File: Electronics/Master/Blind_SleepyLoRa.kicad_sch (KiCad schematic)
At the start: 12 parts, among them J1 Conn_01x04_Socket, J2 Conn_01x04_Socket, J3 Conn_01x04_Socket, SW1 SW_Omron_B3FS

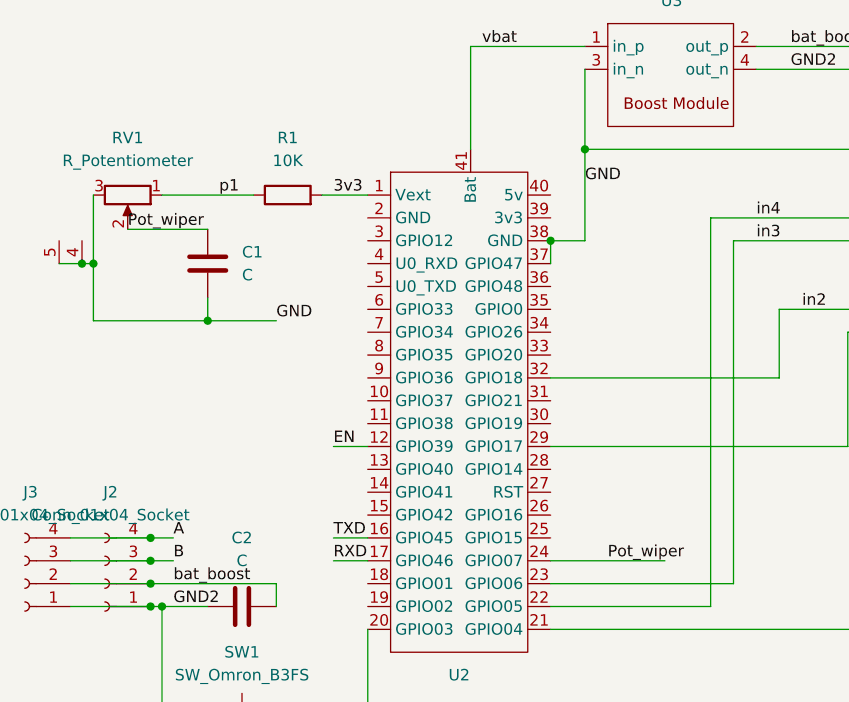
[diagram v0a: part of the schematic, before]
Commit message: Update master PCB to include ref voltage
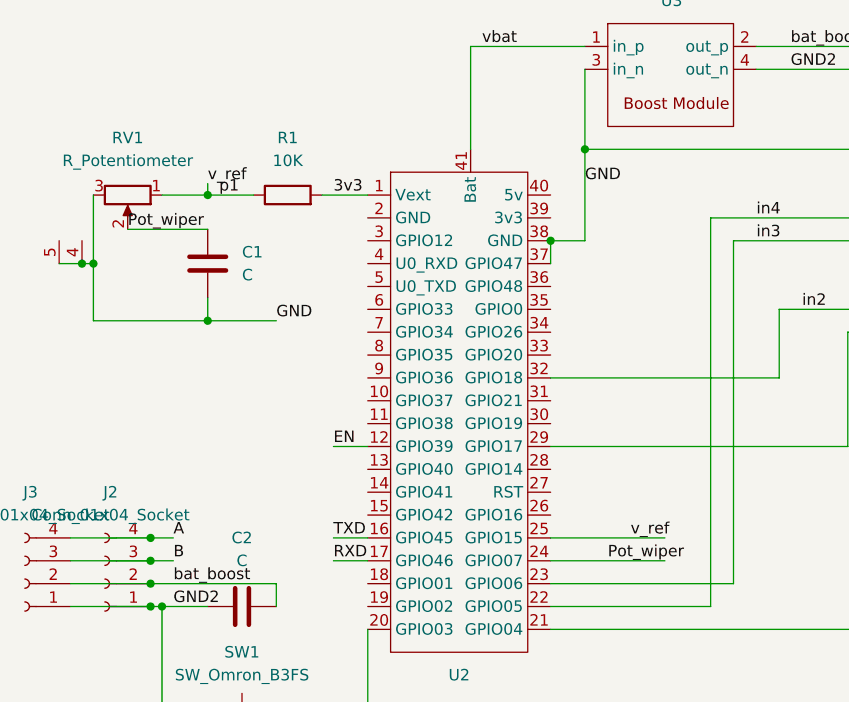
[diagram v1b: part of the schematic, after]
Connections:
- net p1: now also U2.25 (GPIO15)
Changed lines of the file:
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@@
   (junction (at 36.83 86.36) (diameter 0) (color 0 0 0 0)
   )
+  (junction (at 43.18 40.64) (diameter 0) (color 0 0 0 0)
+  )
   (junction (at 29.21 48.26) (diameter 0) (color 0 0 0 0)
   )
@@
     (stroke (width 0) (type default))
   )
+  (wire (pts (xy 81.28 78.74) (xy 93.98 78.74))
+    (stroke (width 0) (type default))
+  )
   (wire (pts (xy 43.18 54.61) (xy 50.8 54.61))
     (stroke (width 0) (type default))
@@
     (stroke (width 0) (type default))
   )
+  (wire (pts (xy 43.18 40.64) (xy 48.26 40.64))
+    (stroke (width 0) (type default))
+  )
   (wire (pts (xy 57.15 81.28) (xy 60.96 81.28))
     (stroke (width 0) (type default))
@@
     (stroke (width 0) (type default))
   )
+  (wire (pts (xy 43.18 39.37) (xy 43.18 40.64))
+    (stroke (width 0) (type default))
+  )
   (wire (pts (xy 101.6 45.72) (xy 127 45.72))
     (stroke (width 0) (type default))
   )
-  (wire (pts (xy 38.1 40.64) (xy 48.26 40.64))
+  (wire (pts (xy 38.1 40.64) (xy 43.18 40.64))
     (stroke (width 0) (type default))
   )
@@
     (effects (font (size 1.27 1.27)) (justify left bottom))
   )
+  (label "v_ref" (at 90.17 78.74 0) (fields_autoplaced)
+    (effects (font (size 1.27 1.27)) (justify left bottom))
+  )
   (label "GND" (at 85.09 110.49 0) (fields_autoplaced)
     (effects (font (size 1.27 1.27)) (justify left bottom))
@@
     (effects (font (size 1.27 1.27)) (justify left bottom))
   )
+  (label "v_ref" (at 43.18 39.37 0) (fields_autoplaced)
+    (effects (font (size 1.27 1.27)) (justify left bottom))
+  )
